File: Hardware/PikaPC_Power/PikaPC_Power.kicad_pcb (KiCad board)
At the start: 2 copper layers, 101.6 x 101.6 mm, 14 parts, among them J1 ATX-24, J2 DIN41612_03x32_C_Split, J3 ATX-20, J4 Conn_01x02, J5 Conn_01x02, SW1 SW_Push_DPDT

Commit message: Un-assign main bus pins 22 & 23
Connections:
- J2 pad b22: GND -> unconnected-(J2B-Pin_b22-Padb22)
- J2 pad b23: GND -> unconnected-(J2B-Pin_b23-Padb23)
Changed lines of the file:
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@@
 	(net 74 "unconnected-(SW1-B-Pad5)")
 	(net 75 "unconnected-(SW1-A-Pad1)")
+	(net 76 "unconnected-(J2B-Pin_b23-Padb23)")
+	(net 77 "unconnected-(J2B-Pin_b22-Padb22)")
 	(footprint "Resistor_THT:R_Array_SIP10"
 		(layer "F.Cu")
@@
 			)
 			(layer "F.SilkS")
-			(net 162414947)
 		)
 		(fp_line
@@
 			)
 			(layer "F.SilkS")
-			(net 162414947)
 		)
 		(fp_line
@@
 			)
 			(layer "F.SilkS")
-			(net 162414947)
 		)
 		(fp_line
@@
 			)
 			(layer "F.SilkS")
-			(net 162414947)
 		)
 		(fp_line
@@
 			)
 			(layer "F.SilkS")
-			(net 162414947)
 		)
 		(fp_line
@@
 			)
 			(layer "F.SilkS")
-			(net 162414947)
 		)
 		(fp_line
@@
 			)
 			(layer "F.SilkS")
-			(net 162414947)
 		)
 		(fp_line
@@
 			)
 			(layer "F.SilkS")
-			(net 162414947)
 		)
 		(fp_line
@@
 			)
 			(layer "F.SilkS")
-			(net 162414947)
 		)
 		(fp_line
@@
 			)
 			(layer "F.SilkS")
-			(net 162414947)
 		)
 		(fp_line
@@
 			)
 			(layer "F.SilkS")
-			(net 162414947)
 		)
 		(fp_line
@@
 			)
 			(layer "F.SilkS")
-			(net 162414947)
 		)
 		(fp_line
@@
 			)
 			(layer "F.SilkS")
-			(net 162414947)
 		)
 		(fp_line
@@
 			)
 			(layer "F.SilkS")
-			(net 162414947)
 		)
 		(fp_line
@@
 			)
 			(layer "F.SilkS")
-			(net 162414947)
 		)
 		(fp_line
@@
 			)
 			(layer "F.SilkS")
-			(net 162414947)
 		)
 		(fp_line
@@
 			)
 			(layer "F.SilkS")
-			(net 162414947)
 		)
 		(fp_line
@@
 			)
 			(layer "F.SilkS")
-			(net 162414947)
 		)
 		(fp_line
@@
 			)
 			(layer "F.SilkS")
-			(net 162414947)
 		)
 		(fp_line
@@
 			)
 			(layer "F.SilkS")
-			(net 162414947)
 		)
 		(fp_line
@@
 			)
 			(layer "F.SilkS")
-			(net 162414947)
 		)
 		(fp_line
@@
 			)
 			(layer "F.SilkS")
-			(net 162414947)
 		)
 		(fp_line
@@
 			)
 			(layer "F.SilkS")
-			(net 162414947)
 		)
 		(fp_line
@@
 			)
 			(layer "F.SilkS")
-			(net 162414947)
 		)
 		(fp_line
@@
 			)
 			(layer "F.SilkS")
-			(net 162414947)
 		)
 		(fp_line
@@
 			)
 			(layer "F.SilkS")
-			(net 162414947)
 		)
 		(fp_line
@@
 			)
 			(layer "F.SilkS")
-			(net 162414947)
 		)
 		(fp_line
@@
 			)
 			(layer "F.SilkS")
-			(net 162414947)
 		)
 		(fp_line
@@
 			)
 			(layer "F.SilkS")
-			(net 162414947)
 		)
 		(fp_line
@@
 			)
 			(layer "F.SilkS")
-			(net 162414947)
 		)
 		(fp_line
@@
 			)
 			(layer "F.SilkS")
-			(net 162414947)
 		)
 		(fp_line
@@
 			)
 			(layer "F.SilkS")
-			(net 162414947)
 		)
 		(fp_line
@@
 			)
 			(layer "F.SilkS")
-			(net 162414947)
 		)
 		(fp_line
@@
 			)
 			(layer "F.SilkS")
-			(net 162414947)
 		)
 		(fp_line
@@
 			)
 			(layer "F.SilkS")
-			(net 162414947)
 		)
 		(fp_line
@@
 			)
 			(layer "F.SilkS")
-			(net 162414947)
 		)
 		(fp_line
@@
 			)
 			(layer "F.SilkS")
-			(net 162414947)
 		)
 		(fp_line
@@
 			)
 			(layer "F.SilkS")
-			(net 162414947)
 		)
 		(fp_line
@@
 			)
 			(layer "F.SilkS")
-			(net 162414947)
 		)
 		(fp_line
@@
 			)
 			(layer "F.SilkS")
-			(net 162414947)
 		)
 		(fp_line
@@
 			)
 			(layer "F.SilkS")
-			(net 162414947)
 		)
 		(fp_line
@@
 			)
 			(layer "F.SilkS")
-			(net 162414947)
 		)
 		(fp_line
@@
 			)
 			(layer "Dwgs.User")
-			(net 162414947)
 		)
 		(fp_line
@@
 			)
 			(layer "Cmts.User")
-			(net 162414947)
 		)
 		(fp_line
@@
 			)
 			(layer "Cmts.User")
-			(net 162414947)
 		)
 		(fp_line
@@
 			)
 			(layer "Cmts.User")
-			(net 162414947)
 		)
 		(fp_line
@@
 			)
 			(layer "F.CrtYd")
-			(net 162414947)
 		)
 		(fp_line
@@
 			)
 			(layer "F.CrtYd")
-			(net 162414947)
 		)
 		(fp_line
@@
 			)
 			(layer "F.CrtYd")
-			(net 162414947)
 		)
 		(fp_line
@@
 			)
 			(layer "F.CrtYd")
-			(net 162414947)
 		)
 		(fp_line
@@
 			)
 			(layer "F.CrtYd")
-			(net 162414947)
 		)
 		(fp_line
@@
 			)
 			(layer "F.CrtYd")
-			(net 162414947)
 		)
 		(fp_line
@@
 			)
 			(layer "F.CrtYd")
-			(net 162414947)
 		)
 		(fp_line
@@
 			)
 			(layer "F.CrtYd")
-			(net 162414947)
 		)
 		(fp_line
@@
 			)
 			(layer "F.Fab")
-			(net 162414947)
 		)
 		(fp_line
@@
 			)
 			(layer "F.Fab")
-			(net 162414947)
 		)
 		(fp_line
@@
 			)
 			(layer "F.Fab")
-			(net 162414947)
 		)
 		(fp_line
@@
 			)
 			(layer "F.Fab")
-			(net 162414947)
 		)
 		(fp_line
@@
 			)
 			(layer "F.Fab")
-			(net 162414947)
 		)
 		(fp_line
@@
 			)
 			(layer "F.Fab")
-			(net 162414947)
 		)
 		(fp_line
@@
 			)
 			(layer "F.Fab")
-			(net 162414947)
 		)
 		(fp_line
@@
 			)
 			(layer "F.Fab")
-			(net 162414947)
 		)
 		(fp_line
@@
 			)
 			(layer "F.Fab")
-			(net 162414947)
 		)
 		(fp_line
@@
 			)
 			(layer "F.Fab")
-			(net 162414947)
 		)
 		(fp_line
@@
 			)
 			(layer "F.Fab")
-			(net 162414947)
 		)
 		(fp_line
@@
 			)
 			(layer "F.Fab")
-			(net 162414947)
 		)
 		(fp_line
@@
 			)
 			(layer "F.Fab")
-			(net 162414947)
 		)
 		(fp_line
@@
 			)
 			(layer "F.Fab")
-			(net 162414947)
 		)
 		(fp_line
@@
 			)
 			(layer "F.Fab")
-			(net 162414947)
 		)
 		(fp_text user "Board edge"
@@
 			(layers "*.Cu" "*.Mask")
 			(remove_unused_layers no)
-			(net 1 "GND")
+			(net 77 "unconnected-(J2B-Pin_b22-Padb22)")
 			(pinfunction "Pin_b22")
 			(pintype "passive")
@@
 			(layers "*.Cu" "*.Mask")
 			(remove_unused_layers no)
-			(net 1 "GND")
+			(net 76 "unconnected-(J2B-Pin_b23-Padb23)")
 			(pinfunction "Pin_b23")
 			(pintype "passive")

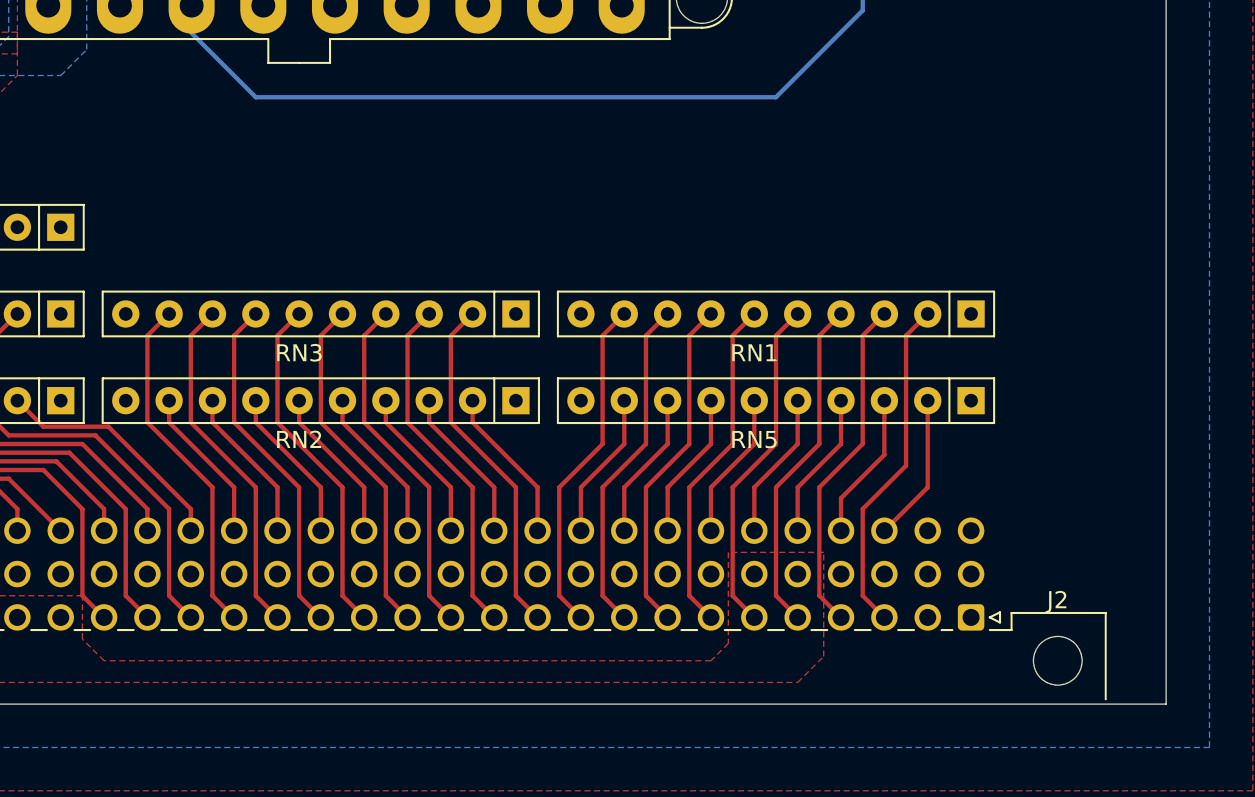
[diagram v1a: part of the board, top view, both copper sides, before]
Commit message: Silkscreen cleanup
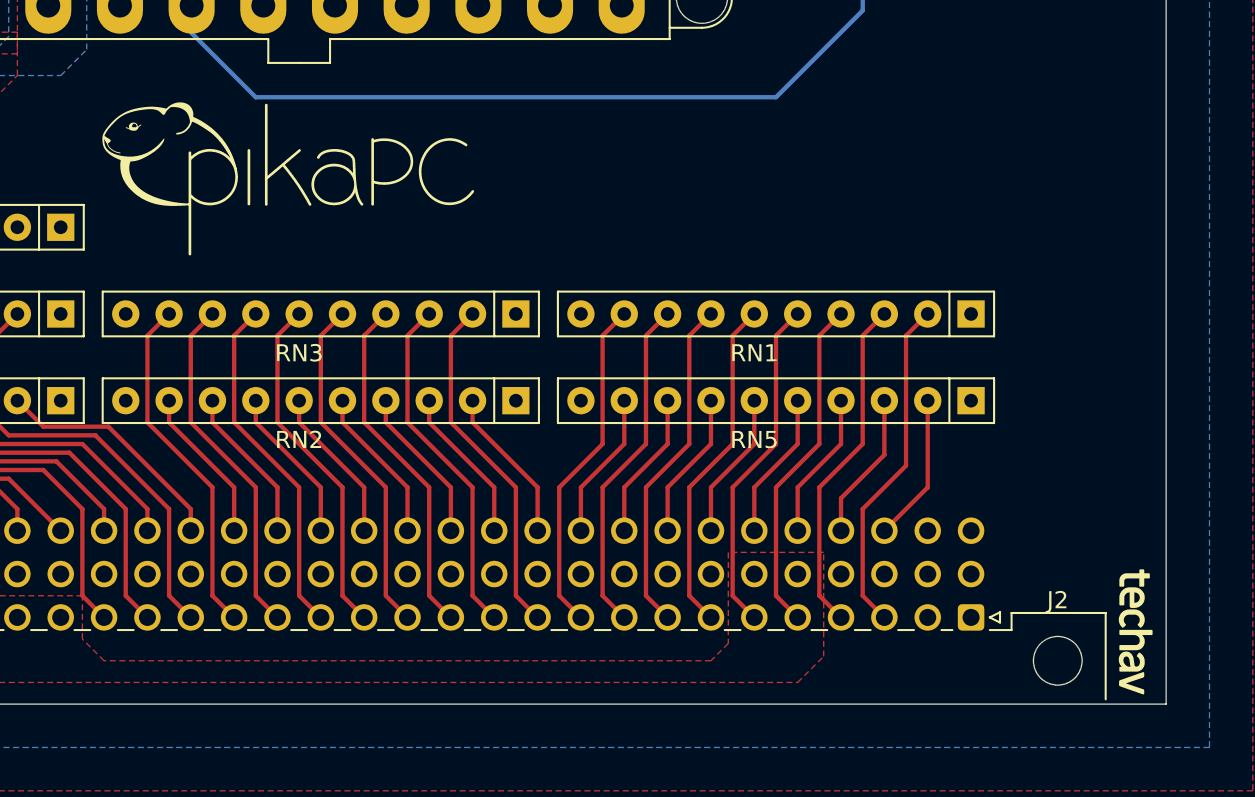
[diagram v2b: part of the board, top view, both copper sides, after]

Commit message: Prep for output
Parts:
- added REF**: PinHeader_1x01_P2.54mm_Vertical, Connector_PinHeader_2.54mm:PinHeader_1x01_P2.54mm_Vertical, F.Cu at (160.0, 66.0)
- added REF**: PinHeader_1x01_P2.54mm_Vertical, Connector_PinHeader_2.54mm:PinHeader_1x01_P2.54mm_Vertical, F.Cu at (86.4, 48.3)
- added REF**: PinHeader_1x01_P2.54mm_Vertical, Connector_PinHeader_2.54mm:PinHeader_1x01_P2.54mm_Vertical, F.Cu at (81.3, 63.5)
- added REF**: PinHeader_1x01_P2.54mm_Vertical, Connector_PinHeader_2.54mm:PinHeader_1x01_P2.54mm_Vertical, F.Cu at (162.6, 68.6)
- added REF**: PinHeader_1x01_P2.54mm_Vertical, Connector_PinHeader_2.54mm:PinHeader_1x01_P2.54mm_Vertical, F.Cu at (86.4, 40.6)
- added REF**: PinHeader_1x01_P2.54mm_Vertical, Connector_PinHeader_2.54mm:PinHeader_1x01_P2.54mm_Vertical, F.Cu at (81.3, 78.7)
- added REF**: PinHeader_1x01_P2.54mm_Vertical, Connector_PinHeader_2.54mm:PinHeader_1x01_P2.54mm_Vertical, F.Cu at (81.3, 76.2)
- added REF**: PinHeader_1x01_P2.54mm_Vertical, Connector_PinHeader_2.54mm:PinHeader_1x01_P2.54mm_Vertical, F.Cu at (94.0, 38.1)
- added REF**: PinHeader_1x01_P2.54mm_Vertical, Connector_PinHeader_2.54mm:PinHeader_1x01_P2.54mm_Vertical, F.Cu at (157.5, 81.3)
- added REF**: PinHeader_1x01_P2.54mm_Vertical, Connector_PinHeader_2.54mm:PinHeader_1x01_P2.54mm_Vertical, F.Cu at (96.5, 50.8)
- added REF**: PinHeader_1x01_P2.54mm_Vertical, Connector_PinHeader_2.54mm:PinHeader_1x01_P2.54mm_Vertical, F.Cu at (78.7, 71.1)
- added REF**: PinHeader_1x01_P2.54mm_Vertical, Connector_PinHeader_2.54mm:PinHeader_1x01_P2.54mm_Vertical, F.Cu at (157.5, 83.8)
- added REF**: PinHeader_1x01_P2.54mm_Vertical, Connector_PinHeader_2.54mm:PinHeader_1x01_P2.54mm_Vertical, F.Cu at (88.9, 35.6)
- added REF**: PinHeader_1x01_P2.54mm_Vertical, Connector_PinHeader_2.54mm:PinHeader_1x01_P2.54mm_Vertical, F.Cu at (160.0, 63.5)
- added REF**: PinHeader_1x01_P2.54mm_Vertical, Connector_PinHeader_2.54mm:PinHeader_1x01_P2.54mm_Vertical, F.Cu at (162.6, 94.0)
- added REF**: PinHeader_1x01_P2.54mm_Vertical, Connector_PinHeader_2.54mm:PinHeader_1x01_P2.54mm_Vertical, F.Cu at (78.7, 43.2)
- added REF**: PinHeader_1x01_P2.54mm_Vertical, Connector_PinHeader_2.54mm:PinHeader_1x01_P2.54mm_Vertical, F.Cu at (167.6, 78.7)
- added REF**: PinHeader_1x01_P2.54mm_Vertical, Connector_PinHeader_2.54mm:PinHeader_1x01_P2.54mm_Vertical, F.Cu at (172.7, 94.0)
- added REF**: PinHeader_1x01_P2.54mm_Vertical, Connector_PinHeader_2.54mm:PinHeader_1x01_P2.54mm_Vertical, F.Cu at (170.2, 94.0)
- added REF**: PinHeader_1x01_P2.54mm_Vertical, Connector_PinHeader_2.54mm:PinHeader_1x01_P2.54mm_Vertical, F.Cu at (94.0, 55.9)
- added REF**: PinHeader_1x01_P2.54mm_Vertical, Connector_PinHeader_2.54mm:PinHeader_1x01_P2.54mm_Vertical, F.Cu at (88.9, 66.0)
- added REF**: PinHeader_1x01_P2.54mm_Vertical, Connector_PinHeader_2.54mm:PinHeader_1x01_P2.54mm_Vertical, F.Cu at (81.3, 48.3)
- added REF**: PinHeader_1x01_P2.54mm_Vertical, Connector_PinHeader_2.54mm:PinHeader_1x01_P2.54mm_Vertical, F.Cu at (86.4, 66.0)
- added REF**: PinHeader_1x01_P2.54mm_Vertical, Connector_PinHeader_2.54mm:PinHeader_1x01_P2.54mm_Vertical, F.Cu at (78.7, 53.3)
- added REF**: PinHeader_1x01_P2.54mm_Vertical, Connector_PinHeader_2.54mm:PinHeader_1x01_P2.54mm_Vertical, F.Cu at (170.2, 71.1)
- added REF**: PinHeader_1x01_P2.54mm_Vertical, Connector_PinHeader_2.54mm:PinHeader_1x01_P2.54mm_Vertical, F.Cu at (172.7, 68.6)
- added REF**: PinHeader_1x01_P2.54mm_Vertical, Connector_PinHeader_2.54mm:PinHeader_1x01_P2.54mm_Vertical, F.Cu at (78.7, 50.8)
- added REF**: PinHeader_1x01_P2.54mm_Vertical, Connector_PinHeader_2.54mm:PinHeader_1x01_P2.54mm_Vertical, F.Cu at (157.5, 68.6)
- added REF**: PinHeader_1x01_P2.54mm_Vertical, Connector_PinHeader_2.54mm:PinHeader_1x01_P2.54mm_Vertical, F.Cu at (96.5, 38.1)
- added REF**: PinHeader_1x01_P2.54mm_Vertical, Connector_PinHeader_2.54mm:PinHeader_1x01_P2.54mm_Vertical, F.Cu at (96.5, 33.0)
- added REF**: PinHeader_1x01_P2.54mm_Vertical, Connector_PinHeader_2.54mm:PinHeader_1x01_P2.54mm_Vertical, F.Cu at (88.9, 61.0)
- added REF**: PinHeader_1x01_P2.54mm_Vertical, Connector_PinHeader_2.54mm:PinHeader_1x01_P2.54mm_Vertical, F.Cu at (162.6, 78.7)
- added REF**: PinHeader_1x01_P2.54mm_Vertical, Connector_PinHeader_2.54mm:PinHeader_1x01_P2.54mm_Vertical, F.Cu at (172.7, 71.1)
- added REF**: PinHeader_1x01_P2.54mm_Vertical, Connector_PinHeader_2.54mm:PinHeader_1x01_P2.54mm_Vertical, F.Cu at (78.7, 76.2)
- added REF**: PinHeader_1x01_P2.54mm_Vertical, Connector_PinHeader_2.54mm:PinHeader_1x01_P2.54mm_Vertical, F.Cu at (160.0, 58.4)
- added REF**: PinHeader_1x01_P2.54mm_Vertical, Connector_PinHeader_2.54mm:PinHeader_1x01_P2.54mm_Vertical, F.Cu at (96.5, 61.0)
- added REF**: PinHeader_1x01_P2.54mm_Vertical, Connector_PinHeader_2.54mm:PinHeader_1x01_P2.54mm_Vertical, F.Cu at (160.0, 61.0)
- added REF**: PinHeader_1x01_P2.54mm_Vertical, Connector_PinHeader_2.54mm:PinHeader_1x01_P2.54mm_Vertical, F.Cu at (78.7, 66.0)
- added REF**: PinHeader_1x01_P2.54mm_Vertical, Connector_PinHeader_2.54mm:PinHeader_1x01_P2.54mm_Vertical, F.Cu at (83.8, 50.8)
- added REF**: PinHeader_1x01_P2.54mm_Vertical, Connector_PinHeader_2.54mm:PinHeader_1x01_P2.54mm_Vertical, F.Cu at (88.9, 58.4)
- added REF**: PinHeader_1x01_P2.54mm_Vertical, Connector_PinHeader_2.54mm:PinHeader_1x01_P2.54mm_Vertical, F.Cu at (91.4, 53.3)
- added REF**: PinHeader_1x01_P2.54mm_Vertical, Connector_PinHeader_2.54mm:PinHeader_1x01_P2.54mm_Vertical, F.Cu at (86.4, 38.1)
- added REF**: PinHeader_1x01_P2.54mm_Vertical, Connector_PinHeader_2.54mm:PinHeader_1x01_P2.54mm_Vertical, F.Cu at (83.8, 30.5)
- added REF**: PinHeader_1x01_P2.54mm_Vertical, Connector_PinHeader_2.54mm:PinHeader_1x01_P2.54mm_Vertical, F.Cu at (157.5, 78.7)
- added REF**: PinHeader_1x01_P2.54mm_Vertical, Connector_PinHeader_2.54mm:PinHeader_1x01_P2.54mm_Vertical, F.Cu at (83.8, 71.1)
- added REF**: PinHeader_1x01_P2.54mm_Vertical, Connector_PinHeader_2.54mm:PinHeader_1x01_P2.54mm_Vertical, F.Cu at (91.4, 50.8)
- added REF**: PinHeader_1x01_P2.54mm_Vertical, Connector_PinHeader_2.54mm:PinHeader_1x01_P2.54mm_Vertical, F.Cu at (167.6, 83.8)
- added REF**: PinHeader_1x01_P2.54mm_Vertical, Connector_PinHeader_2.54mm:PinHeader_1x01_P2.54mm_Vertical, F.Cu at (175.3, 58.4)
- added REF**: PinHeader_1x01_P2.54mm_Vertical, Connector_PinHeader_2.54mm:PinHeader_1x01_P2.54mm_Vertical, F.Cu at (83.8, 35.6)
- added REF**: PinHeader_1x01_P2.54mm_Vertical, Connector_PinHeader_2.54mm:PinHeader_1x01_P2.54mm_Vertical, F.Cu at (83.8, 68.6)
- added REF**: PinHeader_1x01_P2.54mm_Vertical, Connector_PinHeader_2.54mm:PinHeader_1x01_P2.54mm_Vertical, F.Cu at (162.6, 63.5)
- added REF**: PinHeader_1x01_P2.54mm_Vertical, Connector_PinHeader_2.54mm:PinHeader_1x01_P2.54mm_Vertical, F.Cu at (165.1, 61.0)
- added REF**: PinHeader_1x01_P2.54mm_Vertical, Connector_PinHeader_2.54mm:PinHeader_1x01_P2.54mm_Vertical, F.Cu at (88.9, 30.5)
- added REF**: PinHeader_1x01_P2.54mm_Vertical, Connector_PinHeader_2.54mm:PinHeader_1x01_P2.54mm_Vertical, F.Cu at (172.7, 58.4)
- added REF**: PinHeader_1x01_P2.54mm_Vertical, Connector_PinHeader_2.54mm:PinHeader_1x01_P2.54mm_Vertical, F.Cu at (81.3, 61.0)
- added REF**: PinHeader_1x01_P2.54mm_Vertical, Connector_PinHeader_2.54mm:PinHeader_1x01_P2.54mm_Vertical, F.Cu at (167.6, 68.6)
- added REF**: PinHeader_1x01_P2.54mm_Vertical, Connector_PinHeader_2.54mm:PinHeader_1x01_P2.54mm_Vertical, F.Cu at (94.0, 45.7)
- added REF**: PinHeader_1x01_P2.54mm_Vertical, Connector_PinHeader_2.54mm:PinHeader_1x01_P2.54mm_Vertical, F.Cu at (96.5, 55.9)
- added REF**: PinHeader_1x01_P2.54mm_Vertical, Connector_PinHeader_2.54mm:PinHeader_1x01_P2.54mm_Vertical, F.Cu at (175.3, 71.1)
- added REF**: PinHeader_1x01_P2.54mm_Vertical, Connector_PinHeader_2.54mm:PinHeader_1x01_P2.54mm_Vertical, F.Cu at (88.9, 78.7)
- added REF**: PinHeader_1x01_P2.54mm_Vertical, Connector_PinHeader_2.54mm:PinHeader_1x01_P2.54mm_Vertical, F.Cu at (160.0, 81.3)
- added REF**: PinHeader_1x01_P2.54mm_Vertical, Connector_PinHeader_2.54mm:PinHeader_1x01_P2.54mm_Vertical, F.Cu at (88.9, 48.3)
- added REF**: PinHeader_1x01_P2.54mm_Vertical, Connector_PinHeader_2.54mm:PinHeader_1x01_P2.54mm_Vertical, F.Cu at (83.8, 58.4)
- added REF**: PinHeader_1x01_P2.54mm_Vertical, Connector_PinHeader_2.54mm:PinHeader_1x01_P2.54mm_Vertical, F.Cu at (81.3, 53.3)
- added REF**: PinHeader_1x01_P2.54mm_Vertical, Connector_PinHeader_2.54mm:PinHeader_1x01_P2.54mm_Vertical, F.Cu at (172.7, 63.5)
- added REF**: PinHeader_1x01_P2.54mm_Vertical, Connector_PinHeader_2.54mm:PinHeader_1x01_P2.54mm_Vertical, F.Cu at (170.2, 86.4)
- added REF**: PinHeader_1x01_P2.54mm_Vertical, Connector_PinHeader_2.54mm:PinHeader_1x01_P2.54mm_Vertical, F.Cu at (96.5, 45.7)
- added REF**: PinHeader_1x01_P2.54mm_Vertical, Connector_PinHeader_2.54mm:PinHeader_1x01_P2.54mm_Vertical, F.Cu at (165.1, 81.3)
- added REF**: PinHeader_1x01_P2.54mm_Vertical, Connector_PinHeader_2.54mm:PinHeader_1x01_P2.54mm_Vertical, F.Cu at (91.4, 35.6)
- added REF**: PinHeader_1x01_P2.54mm_Vertical, Connector_PinHeader_2.54mm:PinHeader_1x01_P2.54mm_Vertical, F.Cu at (86.4, 45.7)
- added REF**: PinHeader_1x01_P2.54mm_Vertical, Connector_PinHeader_2.54mm:PinHeader_1x01_P2.54mm_Vertical, F.Cu at (165.1, 96.5)
- added REF**: PinHeader_1x01_P2.54mm_Vertical, Connector_PinHeader_2.54mm:PinHeader_1x01_P2.54mm_Vertical, F.Cu at (167.6, 71.1)
- added REF**: PinHeader_1x01_P2.54mm_Vertical, Connector_PinHeader_2.54mm:PinHeader_1x01_P2.54mm_Vertical, F.Cu at (175.3, 76.2)
- added REF**: PinHeader_1x01_P2.54mm_Vertical, Connector_PinHeader_2.54mm:PinHeader_1x01_P2.54mm_Vertical, F.Cu at (96.5, 30.5)
- added REF**: PinHeader_1x01_P2.54mm_Vertical, Connector_PinHeader_2.54mm:PinHeader_1x01_P2.54mm_Vertical, F.Cu at (91.4, 48.3)
- added REF**: PinHeader_1x01_P2.54mm_Vertical, Connector_PinHeader_2.54mm:PinHeader_1x01_P2.54mm_Vertical, F.Cu at (91.4, 61.0)
- added REF**: PinHeader_1x01_P2.54mm_Vertical, Connector_PinHeader_2.54mm:PinHeader_1x01_P2.54mm_Vertical, F.Cu at (167.6, 76.2)
- added REF**: PinHeader_1x01_P2.54mm_Vertical, Connector_PinHeader_2.54mm:PinHeader_1x01_P2.54mm_Vertical, F.Cu at (157.5, 88.9)
- added REF**: PinHeader_1x01_P2.54mm_Vertical, Connector_PinHeader_2.54mm:PinHeader_1x01_P2.54mm_Vertical, F.Cu at (172.7, 76.2)
- added REF**: PinHeader_1x01_P2.54mm_Vertical, Connector_PinHeader_2.54mm:PinHeader_1x01_P2.54mm_Vertical, F.Cu at (81.3, 73.7)
- added REF**: PinHeader_1x01_P2.54mm_Vertical, Connector_PinHeader_2.54mm:PinHeader_1x01_P2.54mm_Vertical, F.Cu at (160.0, 68.6)
- added REF**: PinHeader_1x01_P2.54mm_Vertical, Connector_PinHeader_2.54mm:PinHeader_1x01_P2.54mm_Vertical, F.Cu at (162.6, 91.4)
- added REF**: PinHeader_1x01_P2.54mm_Vertical, Connector_PinHeader_2.54mm:PinHeader_1x01_P2.54mm_Vertical, F.Cu at (175.3, 88.9)
- added REF**: PinHeader_1x01_P2.54mm_Vertical, Connector_PinHeader_2.54mm:PinHeader_1x01_P2.54mm_Vertical, F.Cu at (83.8, 48.3)
- added REF**: PinHeader_1x01_P2.54mm_Vertical, Connector_PinHeader_2.54mm:PinHeader_1x01_P2.54mm_Vertical, F.Cu at (83.8, 66.0)
- added REF**: PinHeader_1x01_P2.54mm_Vertical, Connector_PinHeader_2.54mm:PinHeader_1x01_P2.54mm_Vertical, F.Cu at (81.3, 45.7)
- added REF**: PinHeader_1x01_P2.54mm_Vertical, Connector_PinHeader_2.54mm:PinHeader_1x01_P2.54mm_Vertical, F.Cu at (83.8, 76.2)
- added REF**: PinHeader_1x01_P2.54mm_Vertical, Connector_PinHeader_2.54mm:PinHeader_1x01_P2.54mm_Vertical, F.Cu at (170.2, 63.5)
- added REF**: PinHeader_1x01_P2.54mm_Vertical, Connector_PinHeader_2.54mm:PinHeader_1x01_P2.54mm_Vertical, F.Cu at (81.3, 50.8)
- added REF**: PinHeader_1x01_P2.54mm_Vertical, Connector_PinHeader_2.54mm:PinHeader_1x01_P2.54mm_Vertical, F.Cu at (86.4, 78.7)
- added REF**: PinHeader_1x01_P2.54mm_Vertical, Connector_PinHeader_2.54mm:PinHeader_1x01_P2.54mm_Vertical, F.Cu at (160.0, 73.7)
- added REF**: PinHeader_1x01_P2.54mm_Vertical, Connector_PinHeader_2.54mm:PinHeader_1x01_P2.54mm_Vertical, F.Cu at (83.8, 73.7)
- added REF**: PinHeader_1x01_P2.54mm_Vertical, Connector_PinHeader_2.54mm:PinHeader_1x01_P2.54mm_Vertical, F.Cu at (167.6, 61.0)
- added REF**: PinHeader_1x01_P2.54mm_Vertical, Connector_PinHeader_2.54mm:PinHeader_1x01_P2.54mm_Vertical, F.Cu at (167.6, 63.5)
- added REF**: PinHeader_1x01_P2.54mm_Vertical, Connector_PinHeader_2.54mm:PinHeader_1x01_P2.54mm_Vertical, F.Cu at (81.3, 43.2)
- added REF**: PinHeader_1x01_P2.54mm_Vertical, Connector_PinHeader_2.54mm:PinHeader_1x01_P2.54mm_Vertical, F.Cu at (170.2, 96.5)
- added REF**: PinHeader_1x01_P2.54mm_Vertical, Connector_PinHeader_2.54mm:PinHeader_1x01_P2.54mm_Vertical, F.Cu at (160.0, 96.5)
- added REF**: PinHeader_1x01_P2.54mm_Vertical, Connector_PinHeader_2.54mm:PinHeader_1x01_P2.54mm_Vertical, F.Cu at (83.8, 78.7)
- added REF**: PinHeader_1x01_P2.54mm_Vertical, Connector_PinHeader_2.54mm:PinHeader_1x01_P2.54mm_Vertical, F.Cu at (94.0, 58.4)
- added REF**: PinHeader_1x01_P2.54mm_Vertical, Connector_PinHeader_2.54mm:PinHeader_1x01_P2.54mm_Vertical, F.Cu at (78.7, 63.5)
- added REF**: PinHeader_1x01_P2.54mm_Vertical, Connector_PinHeader_2.54mm:PinHeader_1x01_P2.54mm_Vertical, F.Cu at (91.4, 73.7)
- added REF**: PinHeader_1x01_P2.54mm_Vertical, Connector_PinHeader_2.54mm:PinHeader_1x01_P2.54mm_Vertical, F.Cu at (88.9, 50.8)
- added REF**: PinHeader_1x01_P2.54mm_Vertical, Connector_PinHeader_2.54mm:PinHeader_1x01_P2.54mm_Vertical, F.Cu at (157.5, 63.5)
- added REF**: PinHeader_1x01_P2.54mm_Vertical, Connector_PinHeader_2.54mm:PinHeader_1x01_P2.54mm_Vertical, F.Cu at (175.3, 81.3)
- added REF**: PinHeader_1x01_P2.54mm_Vertical, Connector_PinHeader_2.54mm:PinHeader_1x01_P2.54mm_Vertical, F.Cu at (91.4, 71.1)
- added REF**: PinHeader_1x01_P2.54mm_Vertical, Connector_PinHeader_2.54mm:PinHeader_1x01_P2.54mm_Vertical, F.Cu at (170.2, 76.2)
- added REF**: PinHeader_1x01_P2.54mm_Vertical, Connector_PinHeader_2.54mm:PinHeader_1x01_P2.54mm_Vertical, F.Cu at (165.1, 66.0)
- added REF**: PinHeader_1x01_P2.54mm_Vertical, Connector_PinHeader_2.54mm:PinHeader_1x01_P2.54mm_Vertical, F.Cu at (96.5, 40.6)
- added REF**: PinHeader_1x01_P2.54mm_Vertical, Connector_PinHeader_2.54mm:PinHeader_1x01_P2.54mm_Vertical, F.Cu at (162.6, 73.7)
- added REF**: PinHeader_1x01_P2.54mm_Vertical, Connector_PinHeader_2.54mm:PinHeader_1x01_P2.54mm_Vertical, F.Cu at (91.4, 45.7)
- added REF**: PinHeader_1x01_P2.54mm_Vertical, Connector_PinHeader_2.54mm:PinHeader_1x01_P2.54mm_Vertical, F.Cu at (91.4, 40.6)
- added REF**: PinHeader_1x01_P2.54mm_Vertical, Connector_PinHeader_2.54mm:PinHeader_1x01_P2.54mm_Vertical, F.Cu at (81.3, 71.1)
- added REF**: PinHeader_1x01_P2.54mm_Vertical, Connector_PinHeader_2.54mm:PinHeader_1x01_P2.54mm_Vertical, F.Cu at (172.7, 88.9)
- added REF**: PinHeader_1x01_P2.54mm_Vertical, Connector_PinHeader_2.54mm:PinHeader_1x01_P2.54mm_Vertical, F.Cu at (165.1, 58.4)
- added REF**: PinHeader_1x01_P2.54mm_Vertical, Connector_PinHeader_2.54mm:PinHeader_1x01_P2.54mm_Vertical, F.Cu at (172.7, 91.4)
- added REF**: PinHeader_1x01_P2.54mm_Vertical, Connector_PinHeader_2.54mm:PinHeader_1x01_P2.54mm_Vertical, F.Cu at (83.8, 45.7)
- added REF**: PinHeader_1x01_P2.54mm_Vertical, Connector_PinHeader_2.54mm:PinHeader_1x01_P2.54mm_Vertical, F.Cu at (165.1, 78.7)
- added REF**: PinHeader_1x01_P2.54mm_Vertical, Connector_PinHeader_2.54mm:PinHeader_1x01_P2.54mm_Vertical, F.Cu at (88.9, 33.0)
- added REF**: PinHeader_1x01_P2.54mm_Vertical, Connector_PinHeader_2.54mm:PinHeader_1x01_P2.54mm_Vertical, F.Cu at (170.2, 73.7)
- added REF**: PinHeader_1x01_P2.54mm_Vertical, Connector_PinHeader_2.54mm:PinHeader_1x01_P2.54mm_Vertical, F.Cu at (94.0, 35.6)
- added REF**: PinHeader_1x01_P2.54mm_Vertical, Connector_PinHeader_2.54mm:PinHeader_1x01_P2.54mm_Vertical, F.Cu at (94.0, 63.5)
- added REF**: PinHeader_1x01_P2.54mm_Vertical, Connector_PinHeader_2.54mm:PinHeader_1x01_P2.54mm_Vertical, F.Cu at (175.3, 68.6)
- added REF**: PinHeader_1x01_P2.54mm_Vertical, Connector_PinHeader_2.54mm:PinHeader_1x01_P2.54mm_Vertical, F.Cu at (175.3, 83.8)
- added REF**: PinHeader_1x01_P2.54mm_Vertical, Connector_PinHeader_2.54mm:PinHeader_1x01_P2.54mm_Vertical, F.Cu at (81.3, 58.4)
- added REF**: PinHeader_1x01_P2.54mm_Vertical, Connector_PinHeader_2.54mm:PinHeader_1x01_P2.54mm_Vertical, F.Cu at (94.0, 50.8)
- added REF**: PinHeader_1x01_P2.54mm_Vertical, Connector_PinHeader_2.54mm:PinHeader_1x01_P2.54mm_Vertical, F.Cu at (78.7, 48.3)
- added REF**: PinHeader_1x01_P2.54mm_Vertical, Connector_PinHeader_2.54mm:PinHeader_1x01_P2.54mm_Vertical, F.Cu at (83.8, 61.0)
- added REF**: PinHeader_1x01_P2.54mm_Vertical, Connector_PinHeader_2.54mm:PinHeader_1x01_P2.54mm_Vertical, F.Cu at (94.0, 61.0)
- added REF**: PinHeader_1x01_P2.54mm_Vertical, Connector_PinHeader_2.54mm:PinHeader_1x01_P2.54mm_Vertical, F.Cu at (86.4, 30.5)
- added REF**: PinHeader_1x01_P2.54mm_Vertical, Connector_PinHeader_2.54mm:PinHeader_1x01_P2.54mm_Vertical, F.Cu at (167.6, 96.5)
- added REF**: PinHeader_1x01_P2.54mm_Vertical, Connector_PinHeader_2.54mm:PinHeader_1x01_P2.54mm_Vertical, F.Cu at (170.2, 58.4)
- added REF**: PinHeader_1x01_P2.54mm_Vertical, Connector_PinHeader_2.54mm:PinHeader_1x01_P2.54mm_Vertical, F.Cu at (172.7, 73.7)
- added REF**: PinHeader_1x01_P2.54mm_Vertical, Connector_PinHeader_2.54mm:PinHeader_1x01_P2.54mm_Vertical, F.Cu at (96.5, 58.4)
- added REF**: PinHeader_1x01_P2.54mm_Vertical, Connector_PinHeader_2.54mm:PinHeader_1x01_P2.54mm_Vertical, F.Cu at (162.6, 71.1)
- added REF**: PinHeader_1x01_P2.54mm_Vertical, Connector_PinHeader_2.54mm:PinHeader_1x01_P2.54mm_Vertical, F.Cu at (88.9, 73.7)
- added REF**: PinHeader_1x01_P2.54mm_Vertical, Connector_PinHeader_2.54mm:PinHeader_1x01_P2.54mm_Vertical, F.Cu at (86.4, 76.2)
- added REF**: PinHeader_1x01_P2.54mm_Vertical, Connector_PinHeader_2.54mm:PinHeader_1x01_P2.54mm_Vertical, F.Cu at (83.8, 63.5)
- added REF**: PinHeader_1x01_P2.54mm_Vertical, Connector_PinHeader_2.54mm:PinHeader_1x01_P2.54mm_Vertical, F.Cu at (167.6, 94.0)
- added REF**: PinHeader_1x01_P2.54mm_Vertical, Connector_PinHeader_2.54mm:PinHeader_1x01_P2.54mm_Vertical, F.Cu at (162.6, 86.4)
- added REF**: PinHeader_1x01_P2.54mm_Vertical, Connector_PinHeader_2.54mm:PinHeader_1x01_P2.54mm_Vertical, F.Cu at (165.1, 76.2)
- added REF**: PinHeader_1x01_P2.54mm_Vertical, Connector_PinHeader_2.54mm:PinHeader_1x01_P2.54mm_Vertical, F.Cu at (78.7, 61.0)
- added REF**: PinHeader_1x01_P2.54mm_Vertical, Connector_PinHeader_2.54mm:PinHeader_1x01_P2.54mm_Vertical, F.Cu at (86.4, 71.1)
- added REF**: PinHeader_1x01_P2.54mm_Vertical, Connector_PinHeader_2.54mm:PinHeader_1x01_P2.54mm_Vertical, F.Cu at (167.6, 66.0)
- added REF**: PinHeader_1x01_P2.54mm_Vertical, Connector_PinHeader_2.54mm:PinHeader_1x01_P2.54mm_Vertical, F.Cu at (91.4, 55.9)
- added REF**: PinHeader_1x01_P2.54mm_Vertical, Connector_PinHeader_2.54mm:PinHeader_1x01_P2.54mm_Vertical, F.Cu at (88.9, 38.1)
- added REF**: PinHeader_1x01_P2.54mm_Vertical, Connector_PinHeader_2.54mm:PinHeader_1x01_P2.54mm_Vertical, F.Cu at (83.8, 55.9)
- added REF**: PinHeader_1x01_P2.54mm_Vertical, Connector_PinHeader_2.54mm:PinHeader_1x01_P2.54mm_Vertical, F.Cu at (157.5, 86.4)
- added REF**: PinHeader_1x01_P2.54mm_Vertical, Connector_PinHeader_2.54mm:PinHeader_1x01_P2.54mm_Vertical, F.Cu at (86.4, 50.8)
- added REF**: PinHeader_1x01_P2.54mm_Vertical, Connector_PinHeader_2.54mm:PinHeader_1x01_P2.54mm_Vertical, F.Cu at (86.3, 73.5)
- added REF**: PinHeader_1x01_P2.54mm_Vertical, Connector_PinHeader_2.54mm:PinHeader_1x01_P2.54mm_Vertical, F.Cu at (175.3, 63.5)
- added REF**: PinHeader_1x01_P2.54mm_Vertical, Connector_PinHeader_2.54mm:PinHeader_1x01_P2.54mm_Vertical, F.Cu at (96.5, 53.3)
- added REF**: PinHeader_1x01_P2.54mm_Vertical, Connector_PinHeader_2.54mm:PinHeader_1x01_P2.54mm_Vertical, F.Cu at (170.2, 68.6)
- added REF**: PinHeader_1x01_P2.54mm_Vertical, Connector_PinHeader_2.54mm:PinHeader_1x01_P2.54mm_Vertical, F.Cu at (88.9, 43.2)
- added REF**: PinHeader_1x01_P2.54mm_Vertical, Connector_PinHeader_2.54mm:PinHeader_1x01_P2.54mm_Vertical, F.Cu at (157.5, 91.4)
- added REF**: PinHeader_1x01_P2.54mm_Vertical, Connector_PinHeader_2.54mm:PinHeader_1x01_P2.54mm_Vertical, F.Cu at (88.9, 40.6)
- added REF**: PinHeader_1x01_P2.54mm_Vertical, Connector_PinHeader_2.54mm:PinHeader_1x01_P2.54mm_Vertical, F.Cu at (83.8, 40.6)
- added REF**: PinHeader_1x01_P2.54mm_Vertical, Connector_PinHeader_2.54mm:PinHeader_1x01_P2.54mm_Vertical, F.Cu at (157.5, 71.1)
- added REF**: PinHeader_1x01_P2.54mm_Vertical, Connector_PinHeader_2.54mm:PinHeader_1x01_P2.54mm_Vertical, F.Cu at (83.8, 53.3)
- added REF**: PinHeader_1x01_P2.54mm_Vertical, Connector_PinHeader_2.54mm:PinHeader_1x01_P2.54mm_Vertical, F.Cu at (170.2, 91.4)
- added REF**: PinHeader_1x01_P2.54mm_Vertical, Connector_PinHeader_2.54mm:PinHeader_1x01_P2.54mm_Vertical, F.Cu at (91.4, 33.0)
- added REF**: PinHeader_1x01_P2.54mm_Vertical, Connector_PinHeader_2.54mm:PinHeader_1x01_P2.54mm_Vertical, F.Cu at (175.3, 78.7)
- added REF**: PinHeader_1x01_P2.54mm_Vertical, Connector_PinHeader_2.54mm:PinHeader_1x01_P2.54mm_Vertical, F.Cu at (167.6, 81.3)
- added REF**: PinHeader_1x01_P2.54mm_Vertical, Connector_PinHeader_2.54mm:PinHeader_1x01_P2.54mm_Vertical, F.Cu at (94.0, 78.7)
- added REF**: PinHeader_1x01_P2.54mm_Vertical, Connector_PinHeader_2.54mm:PinHeader_1x01_P2.54mm_Vertical, F.Cu at (86.4, 53.3)
- added REF**: PinHeader_1x01_P2.54mm_Vertical, Connector_PinHeader_2.54mm:PinHeader_1x01_P2.54mm_Vertical, F.Cu at (162.6, 83.8)
- added REF**: PinHeader_1x01_P2.54mm_Vertical, Connector_PinHeader_2.54mm:PinHeader_1x01_P2.54mm_Vertical, F.Cu at (86.4, 55.9)
- added REF**: PinHeader_1x01_P2.54mm_Vertical, Connector_PinHeader_2.54mm:PinHeader_1x01_P2.54mm_Vertical, F.Cu at (81.3, 40.6)
- added REF**: PinHeader_1x01_P2.54mm_Vertical, Connector_PinHeader_2.54mm:PinHeader_1x01_P2.54mm_Vertical, F.Cu at (94.0, 43.2)
- added REF**: PinHeader_1x01_P2.54mm_Vertical, Connector_PinHeader_2.54mm:PinHeader_1x01_P2.54mm_Vertical, F.Cu at (175.3, 96.5)
- added REF**: PinHeader_1x01_P2.54mm_Vertical, Connector_PinHeader_2.54mm:PinHeader_1x01_P2.54mm_Vertical, F.Cu at (96.5, 43.2)
- added REF**: PinHeader_1x01_P2.54mm_Vertical, Connector_PinHeader_2.54mm:PinHeader_1x01_P2.54mm_Vertical, F.Cu at (91.4, 38.1)
- added REF**: PinHeader_1x01_P2.54mm_Vertical, Connector_PinHeader_2.54mm:PinHeader_1x01_P2.54mm_Vertical, F.Cu at (86.4, 63.5)
- added REF**: PinHeader_1x01_P2.54mm_Vertical, Connector_PinHeader_2.54mm:PinHeader_1x01_P2.54mm_Vertical, F.Cu at (91.4, 58.4)
- added REF**: PinHeader_1x01_P2.54mm_Vertical, Connector_PinHeader_2.54mm:PinHeader_1x01_P2.54mm_Vertical, F.Cu at (88.9, 76.2)
- added REF**: PinHeader_1x01_P2.54mm_Vertical, Connector_PinHeader_2.54mm:PinHeader_1x01_P2.54mm_Vertical, F.Cu at (94.0, 71.1)
- added REF**: PinHeader_1x01_P2.54mm_Vertical, Connector_PinHeader_2.54mm:PinHeader_1x01_P2.54mm_Vertical, F.Cu at (78.7, 78.7)
- added REF**: PinHeader_1x01_P2.54mm_Vertical, Connector_PinHeader_2.54mm:PinHeader_1x01_P2.54mm_Vertical, F.Cu at (170.2, 61.0)
- added REF**: PinHeader_1x01_P2.54mm_Vertical, Connector_PinHeader_2.54mm:PinHeader_1x01_P2.54mm_Vertical, F.Cu at (157.5, 61.0)
- added REF**: PinHeader_1x01_P2.54mm_Vertical, Connector_PinHeader_2.54mm:PinHeader_1x01_P2.54mm_Vertical, F.Cu at (88.9, 45.7)
- added REF**: PinHeader_1x01_P2.54mm_Vertical, Connector_PinHeader_2.54mm:PinHeader_1x01_P2.54mm_Vertical, F.Cu at (88.9, 71.1)
- added REF**: PinHeader_1x01_P2.54mm_Vertical, Connector_PinHeader_2.54mm:PinHeader_1x01_P2.54mm_Vertical, F.Cu at (175.3, 91.4)
- added REF**: PinHeader_1x01_P2.54mm_Vertical, Connector_PinHeader_2.54mm:PinHeader_1x01_P2.54mm_Vertical, F.Cu at (165.1, 68.6)
- added REF**: PinHeader_1x01_P2.54mm_Vertical, Connector_PinHeader_2.54mm:PinHeader_1x01_P2.54mm_Vertical, F.Cu at (165.1, 91.4)
- added REF**: PinHeader_1x01_P2.54mm_Vertical, Connector_PinHeader_2.54mm:PinHeader_1x01_P2.54mm_Vertical, F.Cu at (81.3, 68.6)
- added REF**: PinHeader_1x01_P2.54mm_Vertical, Connector_PinHeader_2.54mm:PinHeader_1x01_P2.54mm_Vertical, F.Cu at (165.1, 73.7)
- added REF**: PinHeader_1x01_P2.54mm_Vertical, Connector_PinHeader_2.54mm:PinHeader_1x01_P2.54mm_Vertical, F.Cu at (160.0, 91.4)
- added REF**: PinHeader_1x01_P2.54mm_Vertical, Connector_PinHeader_2.54mm:PinHeader_1x01_P2.54mm_Vertical, F.Cu at (170.2, 83.8)
- added REF**: PinHeader_1x01_P2.54mm_Vertical, Connector_PinHeader_2.54mm:PinHeader_1x01_P2.54mm_Vertical, F.Cu at (83.8, 33.0)
- added REF**: PinHeader_1x01_P2.54mm_Vertical, Connector_PinHeader_2.54mm:PinHeader_1x01_P2.54mm_Vertical, F.Cu at (91.4, 78.7)
- added REF**: PinHeader_1x01_P2.54mm_Vertical, Connector_PinHeader_2.54mm:PinHeader_1x01_P2.54mm_Vertical, F.Cu at (91.4, 30.5)
- added REF**: PinHeader_1x01_P2.54mm_Vertical, Connector_PinHeader_2.54mm:PinHeader_1x01_P2.54mm_Vertical, F.Cu at (167.6, 88.9)
- added REF**: PinHeader_1x01_P2.54mm_Vertical, Connector_PinHeader_2.54mm:PinHeader_1x01_P2.54mm_Vertical, F.Cu at (157.5, 94.0)
- added REF**: PinHeader_1x01_P2.54mm_Vertical, Connector_PinHeader_2.54mm:PinHeader_1x01_P2.54mm_Vertical, F.Cu at (160.0, 76.2)
- added REF**: PinHeader_1x01_P2.54mm_Vertical, Connector_PinHeader_2.54mm:PinHeader_1x01_P2.54mm_Vertical, F.Cu at (78.7, 40.6)
- added REF**: PinHeader_1x01_P2.54mm_Vertical, Connector_PinHeader_2.54mm:PinHeader_1x01_P2.54mm_Vertical, F.Cu at (165.1, 86.4)
- added REF**: PinHeader_1x01_P2.54mm_Vertical, Connector_PinHeader_2.54mm:PinHeader_1x01_P2.54mm_Vertical, F.Cu at (91.4, 43.2)
- added REF**: PinHeader_1x01_P2.54mm_Vertical, Connector_PinHeader_2.54mm:PinHeader_1x01_P2.54mm_Vertical, F.Cu at (78.7, 45.7)
- added REF**: PinHeader_1x01_P2.54mm_Vertical, Connector_PinHeader_2.54mm:PinHeader_1x01_P2.54mm_Vertical, F.Cu at (175.3, 94.0)
- added REF**: PinHeader_1x01_P2.54mm_Vertical, Connector_PinHeader_2.54mm:PinHeader_1x01_P2.54mm_Vertical, F.Cu at (167.6, 91.4)
- added REF**: PinHeader_1x01_P2.54mm_Vertical, Connector_PinHeader_2.54mm:PinHeader_1x01_P2.54mm_Vertical, F.Cu at (88.9, 68.6)
- added REF**: PinHeader_1x01_P2.54mm_Vertical, Connector_PinHeader_2.54mm:PinHeader_1x01_P2.54mm_Vertical, F.Cu at (162.6, 96.5)
- added REF**: PinHeader_1x01_P2.54mm_Vertical, Connector_PinHeader_2.54mm:PinHeader_1x01_P2.54mm_Vertical, F.Cu at (175.3, 66.0)
- added REF**: PinHeader_1x01_P2.54mm_Vertical, Connector_PinHeader_2.54mm:PinHeader_1x01_P2.54mm_Vertical, F.Cu at (88.9, 63.5)
- added REF**: PinHeader_1x01_P2.54mm_Vertical, Connector_PinHeader_2.54mm:PinHeader_1x01_P2.54mm_Vertical, F.Cu at (94.0, 30.5)
- added REF**: PinHeader_1x01_P2.54mm_Vertical, Connector_PinHeader_2.54mm:PinHeader_1x01_P2.54mm_Vertical, F.Cu at (86.4, 61.0)
- added REF**: PinHeader_1x01_P2.54mm_Vertical, Connector_PinHeader_2.54mm:PinHeader_1x01_P2.54mm_Vertical, F.Cu at (83.8, 38.1)
- added REF**: PinHeader_1x01_P2.54mm_Vertical, Connector_PinHeader_2.54mm:PinHeader_1x01_P2.54mm_Vertical, F.Cu at (172.7, 81.3)
- added REF**: PinHeader_1x01_P2.54mm_Vertical, Connector_PinHeader_2.54mm:PinHeader_1x01_P2.54mm_Vertical, F.Cu at (78.7, 58.4)
- added REF**: PinHeader_1x01_P2.54mm_Vertical, Connector_PinHeader_2.54mm:PinHeader_1x01_P2.54mm_Vertical, F.Cu at (78.7, 68.6)
- added REF**: PinHeader_1x01_P2.54mm_Vertical, Connector_PinHeader_2.54mm:PinHeader_1x01_P2.54mm_Vertical, F.Cu at (94.0, 33.0)
- added REF**: PinHeader_1x01_P2.54mm_Vertical, Connector_PinHeader_2.54mm:PinHeader_1x01_P2.54mm_Vertical, F.Cu at (160.0, 86.4)
- added REF**: PinHeader_1x01_P2.54mm_Vertical, Connector_PinHeader_2.54mm:PinHeader_1x01_P2.54mm_Vertical, F.Cu at (81.3, 66.0)
- added REF**: PinHeader_1x01_P2.54mm_Vertical, Connector_PinHeader_2.54mm:PinHeader_1x01_P2.54mm_Vertical, F.Cu at (157.5, 76.2)
- added REF**: PinHeader_1x01_P2.54mm_Vertical, Connector_PinHeader_2.54mm:PinHeader_1x01_P2.54mm_Vertical, F.Cu at (157.5, 96.5)
- added REF**: PinHeader_1x01_P2.54mm_Vertical, Connector_PinHeader_2.54mm:PinHeader_1x01_P2.54mm_Vertical, F.Cu at (172.7, 86.4)
- added REF**: PinHeader_1x01_P2.54mm_Vertical, Connector_PinHeader_2.54mm:PinHeader_1x01_P2.54mm_Vertical, F.Cu at (172.7, 61.0)
- added REF**: PinHeader_1x01_P2.54mm_Vertical, Connector_PinHeader_2.54mm:PinHeader_1x01_P2.54mm_Vertical, F.Cu at (78.7, 55.9)
- added REF**: PinHeader_1x01_P2.54mm_Vertical, Connector_PinHeader_2.54mm:PinHeader_1x01_P2.54mm_Vertical, F.Cu at (91.4, 66.0)
- added REF**: PinHeader_1x01_P2.54mm_Vertical, Connector_PinHeader_2.54mm:PinHeader_1x01_P2.54mm_Vertical, F.Cu at (170.2, 78.7)
- added REF**: PinHeader_1x01_P2.54mm_Vertical, Connector_PinHeader_2.54mm:PinHeader_1x01_P2.54mm_Vertical, F.Cu at (165.1, 88.9)
- added REF**: PinHeader_1x01_P2.54mm_Vertical, Connector_PinHeader_2.54mm:PinHeader_1x01_P2.54mm_Vertical, F.Cu at (160.0, 94.0)
- added REF**: PinHeader_1x01_P2.54mm_Vertical, Connector_PinHeader_2.54mm:PinHeader_1x01_P2.54mm_Vertical, F.Cu at (157.5, 73.7)
- added REF**: PinHeader_1x01_P2.54mm_Vertical, Connector_PinHeader_2.54mm:PinHeader_1x01_P2.54mm_Vertical, F.Cu at (165.1, 83.8)
- added REF**: PinHeader_1x01_P2.54mm_Vertical, Connector_PinHeader_2.54mm:PinHeader_1x01_P2.54mm_Vertical, F.Cu at (88.9, 53.3)
- added REF**: PinHeader_1x01_P2.54mm_Vertical, Connector_PinHeader_2.54mm:PinHeader_1x01_P2.54mm_Vertical, F.Cu at (88.9, 55.9)
- added REF**: PinHeader_1x01_P2.54mm_Vertical, Connector_PinHeader_2.54mm:PinHeader_1x01_P2.54mm_Vertical, F.Cu at (172.7, 78.7)
- added REF**: PinHeader_1x01_P2.54mm_Vertical, Connector_PinHeader_2.54mm:PinHeader_1x01_P2.54mm_Vertical, F.Cu at (162.6, 81.3)
- added REF**: PinHeader_1x01_P2.54mm_Vertical, Connector_PinHeader_2.54mm:PinHeader_1x01_P2.54mm_Vertical, F.Cu at (157.5, 66.0)
- added REF**: PinHeader_1x01_P2.54mm_Vertical, Connector_PinHeader_2.54mm:PinHeader_1x01_P2.54mm_Vertical, F.Cu at (94.0, 76.2)
- added REF**: PinHeader_1x01_P2.54mm_Vertical, Connector_PinHeader_2.54mm:PinHeader_1x01_P2.54mm_Vertical, F.Cu at (162.6, 61.0)
- added REF**: PinHeader_1x01_P2.54mm_Vertical, Connector_PinHeader_2.54mm:PinHeader_1x01_P2.54mm_Vertical, F.Cu at (170.2, 81.3)
- added REF**: PinHeader_1x01_P2.54mm_Vertical, Connector_PinHeader_2.54mm:PinHeader_1x01_P2.54mm_Vertical, F.Cu at (94.0, 68.6)
- added REF**: PinHeader_1x01_P2.54mm_Vertical, Connector_PinHeader_2.54mm:PinHeader_1x01_P2.54mm_Vertical, F.Cu at (91.4, 76.2)
- added REF**: PinHeader_1x01_P2.54mm_Vertical, Connector_PinHeader_2.54mm:PinHeader_1x01_P2.54mm_Vertical, F.Cu at (162.6, 58.4)
- added REF**: PinHeader_1x01_P2.54mm_Vertical, Connector_PinHeader_2.54mm:PinHeader_1x01_P2.54mm_Vertical, F.Cu at (162.6, 76.2)
- added REF**: PinHeader_1x01_P2.54mm_Vertical, Connector_PinHeader_2.54mm:PinHeader_1x01_P2.54mm_Vertical, F.Cu at (86.4, 35.6)
- added REF**: PinHeader_1x01_P2.54mm_Vertical, Connector_PinHeader_2.54mm:PinHeader_1x01_P2.54mm_Vertical, F.Cu at (165.1, 71.1)
- added REF**: PinHeader_1x01_P2.54mm_Vertical, Connector_PinHeader_2.54mm:PinHeader_1x01_P2.54mm_Vertical, F.Cu at (160.0, 78.7)
- added REF**: PinHeader_1x01_P2.54mm_Vertical, Connector_PinHeader_2.54mm:PinHeader_1x01_P2.54mm_Vertical, F.Cu at (160.0, 71.1)
- added REF**: PinHeader_1x01_P2.54mm_Vertical, Connector_PinHeader_2.54mm:PinHeader_1x01_P2.54mm_Vertical, F.Cu at (170.2, 88.9)
- added REF**: PinHeader_1x01_P2.54mm_Vertical, Connector_PinHeader_2.54mm:PinHeader_1x01_P2.54mm_Vertical, F.Cu at (157.5, 58.4)
- added REF**: PinHeader_1x01_P2.54mm_Vertical, Connector_PinHeader_2.54mm:PinHeader_1x01_P2.54mm_Vertical, F.Cu at (94.0, 53.3)
- added REF**: PinHeader_1x01_P2.54mm_Vertical, Connector_PinHeader_2.54mm:PinHeader_1x01_P2.54mm_Vertical, F.Cu at (175.3, 86.4)
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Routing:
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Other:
- board text added: "+12V"
- board text added: "+3.3V"
- board text added: "+5V"
- board text added: "-12V"
- board text added: "GND"
